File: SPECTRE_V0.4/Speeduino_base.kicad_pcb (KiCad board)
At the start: 2 copper layers, 100 x 93 mm, 172 parts, among them J1 Conn_01x04_Male, Q1 2N7002, Q10 BSP78, Q11 BSP78, Q12 BSP78, Q13 BSP78, Q14 BSP78, Q15 BSP78, Q16 BSP78, Q17 BSP78, Q18 BSP78, Q2 CJ2302, Q3 CJ2302, Q4 CJ2302, Q5 BSP78, Q6 BSP78, Q7 CJ2302, Q8 CJ2302, Q9 CJ2302, U1 MAX9926UAEE+, U2 molex_48pin, U3 LM78M05_TO220

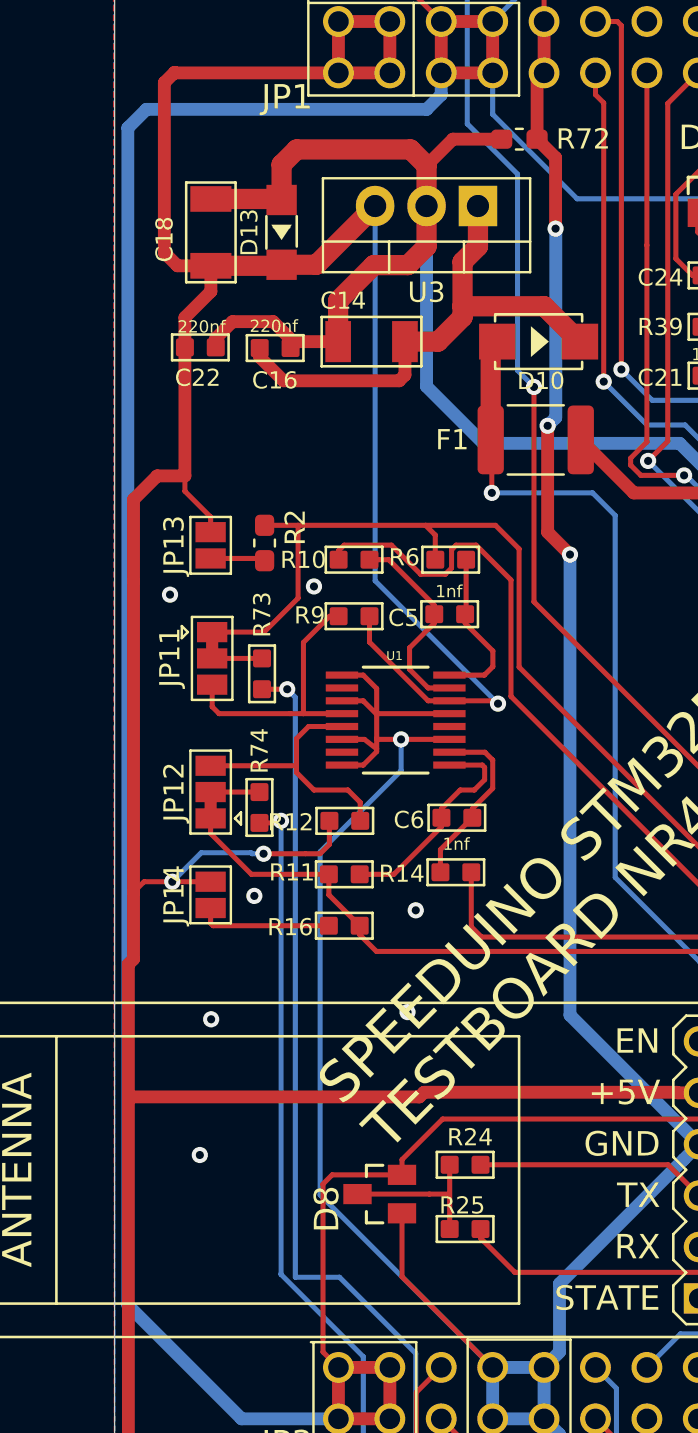
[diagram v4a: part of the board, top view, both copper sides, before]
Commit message: Add zener for safety on 3.3v. All bat54S diodes dump current on 3.3V line when driven above 3.6V therefor the 3.3V needed protection
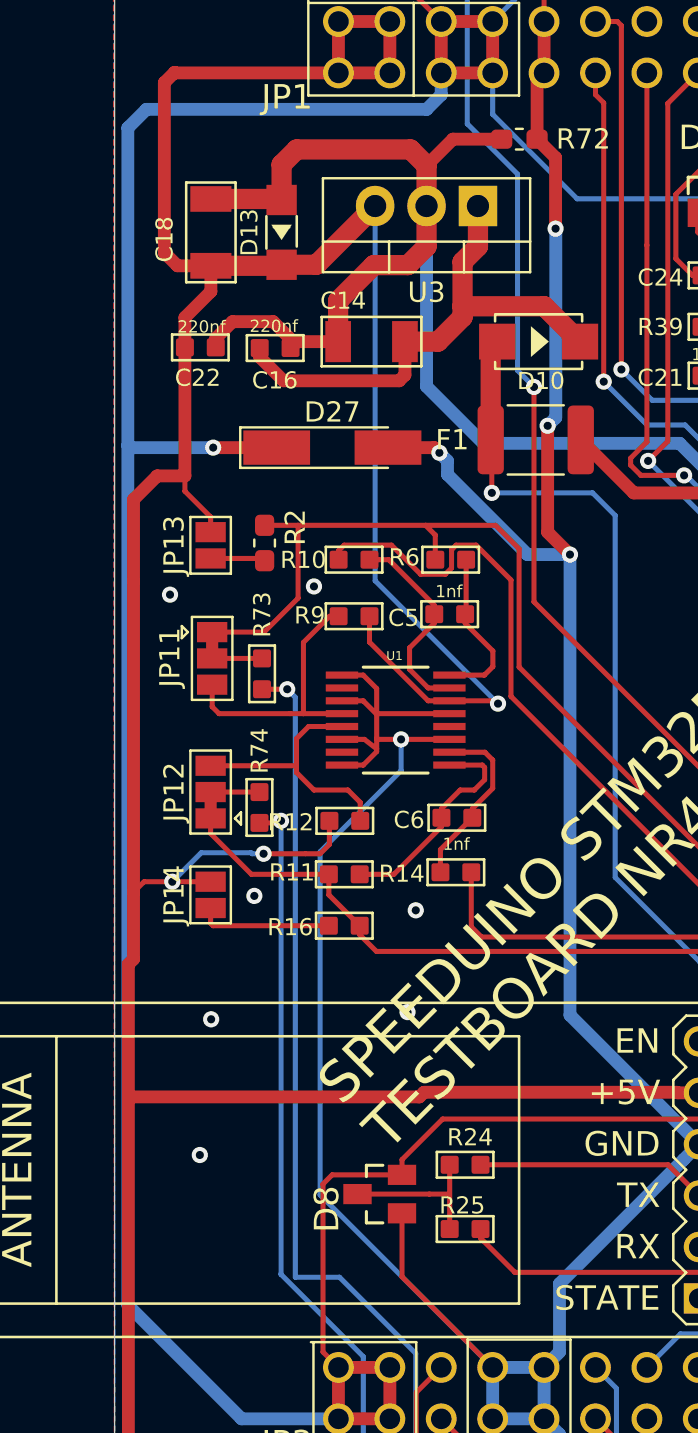
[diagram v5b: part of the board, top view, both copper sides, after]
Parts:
- added D27: 3.6V, Diode_SMD:D_MiniMELF_Handsoldering, F.Cu at (124.8, 49.8)
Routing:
- net GND: track 527.4 -> 539.0 mm, vias 41 -> 42
- net 3.3V: track 540.1 -> 547.5 mm, vias 12 -> 13
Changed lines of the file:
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@@
     (thickness 1.6)
     (drawings 31)
-    (tracks 2179)
+    (tracks 2192)
     (zones 0)
-    (modules 172)
+    (modules 173)
     (nets 173)
   )
@@
   )
   (setup
-    (last_trace_width 0.25)
+    (last_trace_width 0.635)
     (user_trace_width 0.2)
     (user_trace_width 0.45)
@@
     (add_net V_IDLE)
   )
+  (module Diode_SMD:D_MiniMELF_Handsoldering (layer Top)
+    (at 124.758 49.784)
+    (descr "Diode Mini-MELF Handsoldering")
+    (tags "Diode Mini-MELF Handsoldering")
+    (attr smd)
+    (fp_text reference D27 (at 0 -1.75) (layer F.SilkS)
+      (effects (font (size 1 1) (thickness 0.15)))
+    )
+    (fp_text value 3.6V (at 0 1.75) (layer F.Fab)
+      (effects (font (size 1 1) (thickness 0.15)))
+    )
+    (fp_line (start -4.65 1.1) (end -4.65 -1.1) (layer F.CrtYd) (width 0.05))
+    (fp_line (start 4.65 1.1) (end -4.65 1.1) (layer F.CrtYd) (width 0.05))
+    (fp_line (start 4.65 -1.1) (end 4.65 1.1) (layer F.CrtYd) (width 0.05))
+    (fp_line (start -4.65 -1.1) (end 4.65 -1.1) (layer F.CrtYd) (width 0.05))
+    (fp_line (start -0.75 0) (end -0.35 0) (layer F.Fab) (width 0.1))
+    (fp_line (start -0.35 0) (end -0.35 -0.55) (layer F.Fab) (width 0.1))
+    (fp_line (start -0.35 0) (end -0.35 0.55) (layer F.Fab) (width 0.1))
+    (fp_line (start -0.35 0) (end 0.25 -0.4) (layer F.Fab) (width 0.1))
+    (fp_line (start 0.25 -0.4) (end 0.25 0.4) (layer F.Fab) (width 0.1))
+    (fp_line (start 0.25 0.4) (end -0.35 0) (layer F.Fab) (width 0.1))
+    (fp_line (start 0.25 0) (end 0.75 0) (layer F.Fab) (width 0.1))
+    (fp_line (start -1.65 -0.8) (end 1.65 -0.8) (layer F.Fab) (width 0.1))
+    (fp_line (start -1.65 0.8) (end -1.65 -0.8) (layer F.Fab) (width 0.1))
+    (fp_line (start 1.65 0.8) (end -1.65 0.8) (layer F.Fab) (width 0.1))
+    (fp_line (start 1.65 -0.8) (end 1.65 0.8) (layer F.Fab) (width 0.1))
+    (fp_line (start -4.55 1) (end 2.75 1) (layer F.SilkS) (width 0.12))
+    (fp_line (start -4.55 -1) (end -4.55 1) (layer F.SilkS) (width 0.12))
+    (fp_line (start 2.75 -1) (end -4.55 -1) (layer F.SilkS) (width 0.12))
+    (fp_text user %R (at 0 -1.75) (layer F.Fab)
+      (effects (font (size 1 1) (thickness 0.15)))
+    )
+    (pad 2 smd rect (at 2.75 0) (size 3.3 1.7) (layers Top F.Paste F.Mask)
+      (net 1 GND))
+    (pad 1 smd rect (at -2.75 0) (size 3.3 1.7) (layers Top F.Paste F.Mask)
+      (net 66 3.3V))
+    (model ${KISYS3DMOD}/Diode_SMD.3dshapes/D_MiniMELF.wrl
+      (at (xyz 0 0 0))
+      (scale (xyz 1 1 1))
+      (rotate (xyz 0 0 0))
+    )
+  )
   (module Speeduino_base:SOT223 (layer Bottom)
     (at 190.957 69.051712 90)
@@
     (effects (font (size 0.77216 0.77216) (thickness 0.065024)) (justify left bottom))
   )
-  (via (at 210.6168 94.2848) (size 0.8) (drill 0.4) (layers Top Bottom) (net 34))
-  (via (at 206.756 97.9424) (size 0.8) (drill 0.4) (layers Top Bottom) (net 34))
   (via (at 205.3844 53.7972) (size 0.8) (drill 0.4) (layers Top Bottom) (net 0))
   (segment (start 135.22 28.73) (end 135.22 31.27) (width 0.635) (layer Top) (net 1) (status 30))
@@
   (via (at 164.6936 69.7484) (size 0.8) (drill 0.4) (layers Top Bottom) (net 1))
   (via (at 159.9184 68.6816) (size 0.8) (drill 0.4) (layers Top Bottom) (net 1))
+  (via (at 130.048 50.038) (size 0.8) (drill 0.4) (layers Top Bottom) (net 1))
+  (segment (start 127.508 49.784) (end 129.794 49.784) (width 0.635) (layer Top) (net 1))
+  (segment (start 129.794 49.784) (end 130.048 50.038) (width 0.635) (layer Top) (net 1))
+  (segment (start 134.402898 55.0672) (end 135.933915 55.0672) (width 0.635) (layer Bottom) (net 1))
+  (segment (start 130.447999 51.112301) (end 134.402898 55.0672) (width 0.635) (layer Bottom) (net 1))
+  (segment (start 130.447999 50.437999) (end 130.447999 51.112301) (width 0.635) (layer Bottom) (net 1))
+  (segment (start 135.933915 55.0672) (end 136.4996 55.0672) (width 0.635) (layer Bottom) (net 1))
+  (segment (start 130.048 50.038) (end 130.447999 50.437999) (width 0.635) (layer Bottom) (net 1))
   (segment (start 157.2717 79.121) (end 157.3021 79.0906) (width 0.25) (layer Top) (net 2))
   (segment (start 151.5872 79.0956) (end 152.5524 79.0956) (width 0.25) (layer Top) (net 2))
@@
   (segment (start 154.432 71.374) (end 155.0924 71.374) (width 0.25) (layer Top) (net 31))
   (segment (start 155.0924 71.374) (end 155.2956 71.1708) (width 0.25) (layer Top) (net 31))
+  (via (at 210.6168 94.2848) (size 0.8) (drill 0.4) (layers Top Bottom) (net 34))
+  (via (at 206.756 97.9424) (size 0.8) (drill 0.4) (layers Top Bottom) (net 34))
   (segment (start 206.883 48.217) (end 206.81 48.29) (width 0.635) (layer Bottom) (net 34) (status 30))
   (segment (start 204.27 48.29) (end 206.81 48.29) (width 1.6) (layer Bottom) (net 34) (status 30))
@@
   (segment (start 130.14 31.27) (end 130.14 32.34763) (width 0.635) (layer Bottom) (net 66))
   (segment (start 115.57 33.0708) (end 114.6556 33.9852) (width 0.635) (layer Bottom) (net 66))
-  (segment (start 114.6556 33.9852) (end 114.6556 92.1512) (width 0.635) (layer Bottom) (net 66))
   (segment (start 114.6556 92.1512) (end 120.2744 97.77) (width 0.635) (layer Bottom) (net 66))
   (via (at 146.2024 37.4904) (size 0.8) (drill 0.4) (layers Top Bottom) (net 66))
@@
   (segment (start 120.9548 25.5016) (end 120.9548 23.7744) (width 0.25) (layer Top) (net 66))
   (segment (start 127.9784 26.5684) (end 122.0216 26.5684) (width 0.25) (layer Top) (net 66))
+  (via (at 118.872 49.784) (size 0.8) (drill 0.4) (layers Top Bottom) (net 66))
+  (segment (start 122.008 49.784) (end 118.872 49.784) (width 0.635) (layer Top) (net 66))
+  (segment (start 114.6556 49.6824) (end 114.7572 49.784) (width 0.635) (layer Bottom) (net 66))
+  (segment (start 114.7572 49.784) (end 118.872 49.784) (width 0.635) (layer Bottom) (net 66))
+  (segment (start 114.6556 49.6824) (end 114.6556 92.1512) (width 0.635) (layer Bottom) (net 66))
+  (segment (start 114.6556 33.9852) (end 114.6556 49.6824) (width 0.635) (layer Bottom) (net 66))
   (segment (start 199.19 78.35) (end 184.159 78.35) (width 0.25) (layer Top) (net 67) (status 10))
   (segment (start 184.159 78.35) (end 178.3932 78.35) (width 0.25) (layer Top) (net 67))
@@
   )
   (zone (net 34) (net_name PWR_GND) (layer Bottom) (hatch edge 0.508)
-    (connect_pads yes (clearance 0.254))
+    (connect_pads (clearance 0.254))
     (min_thickness 0.254)
     (fill yes (arc_segments 32) (thermal_gap 0.508) (thermal_bridge_width 0.508))
@@
   )
   (zone (net 34) (net_name PWR_GND) (layer Top) (hatch edge 0.508)
-    (connect_pads yes (clearance 0.254))
+    (connect_pads (clearance 0.254))
     (min_thickness 0.254)
     (fill yes (arc_segments 32) (thermal_gap 0.508) (thermal_bridge_width 0.508))
@@
   (zone (net 1) (net_name GND) (layer Top) (hatch edge 0.508)
     (priority 1)
-    (connect_pads yes (clearance 0.254))
+    (connect_pads (clearance 0.254))
     (min_thickness 0.254)
     (fill yes (arc_segments 32) (thermal_gap 0.508) (thermal_bridge_width 0.508))
@@
   (zone (net 1) (net_name GND) (layer Bottom) (hatch edge 0.508)
     (priority 1)
-    (connect_pads yes (clearance 0.254))
+    (connect_pads (clearance 0.254))
     (min_thickness 0.254)
     (fill yes (arc_segments 32) (thermal_gap 0.508) (thermal_bridge_width 0.508))

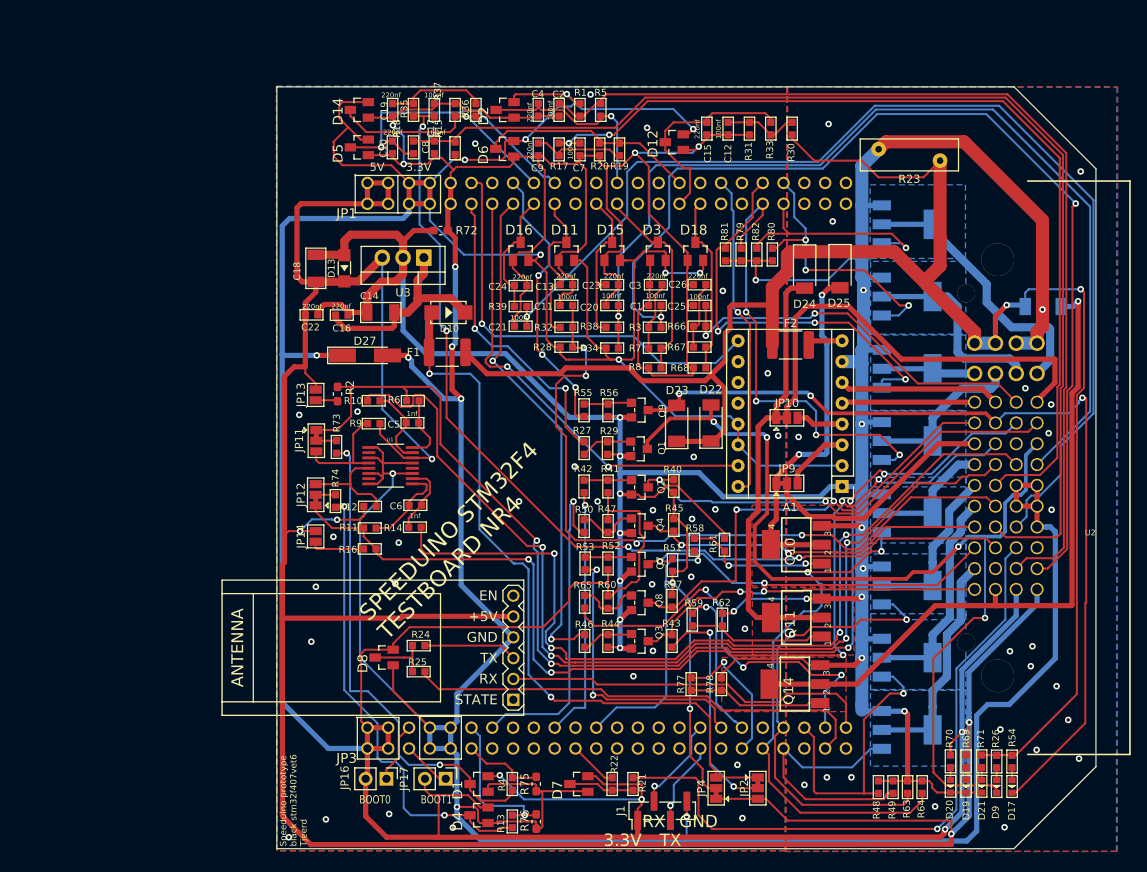
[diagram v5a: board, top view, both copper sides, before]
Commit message: add canbus driver add 3d models to components for 3d render.
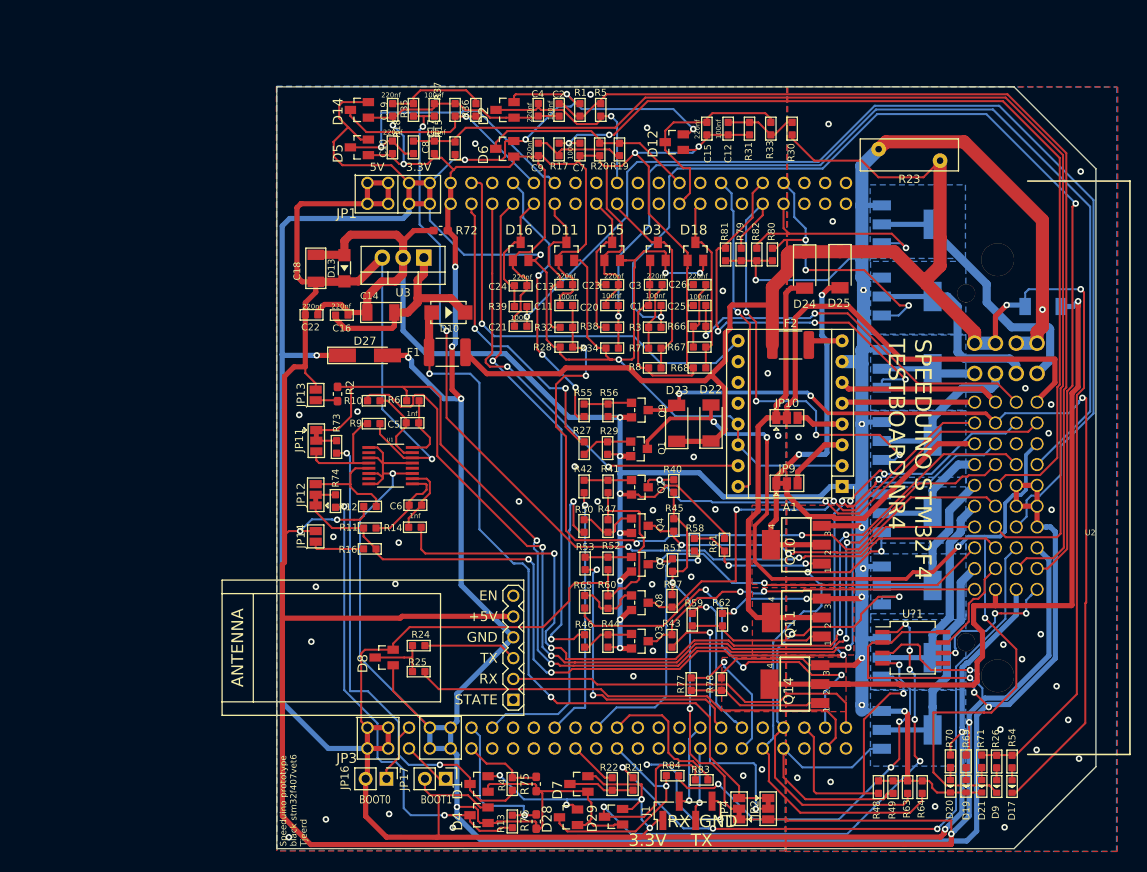
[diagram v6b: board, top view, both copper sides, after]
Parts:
- added D28: BAT54S, Speeduino_base:SOT23, F.Cu at (149.6, 106.2)
- added D29: BAT54S, Speeduino_base:SOT23, F.Cu at (155.1, 106.1)
- added R83: 1k, Speeduino_base:R0603, F.Cu at (165.9, 101.6)
- added R84: 1K, Speeduino_base:R0603, F.Cu at (162.3, 101.1)
- added U?1: TJA1050, Package_SO:SO-8_5.3x6.2mm_P1.27mm, F.Cu at (191.6, 85.5)
- D22, D23, D24, D25, D26: footprint Diode_SMD:D_SOD-128 -> Speeduino_base:D_SOD-128
- moved JP4 3.76 mm to (170.4, 105.1)
- moved J1 3.08 mm to (164.1, 105.4)
- moved JP2 2.81 mm to (174.0, 105.1)
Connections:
- U2 pad 37: Net-(U2-Pad37) -> 5V
- U2 pad 43: Net-(U2-Pad43) -> CANH
- U2 pad 45: 5V -> CANL
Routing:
- net Net-(D29-Pad3): track 0.00 -> 83.3 mm, vias 0 -> 6
- net GND: track 539.0 -> 591.8 mm, vias 42 -> 46
- net Net-(R84-Pad2): track 0.00 -> 47.8 mm, vias 0 -> 4
- net PD0: track 0.00 -> 26.7 mm, vias 0 -> 1
- net 5V: track 342.6 -> 364.5 mm, vias 5 -> 6
- net CANL: track 0.00 -> 18.8 mm, vias 0 -> 3
- net PD1: track 0.00 -> 17.5 mm
- net CANH: track 0.00 -> 12.4 mm
- net BOOST-OUT: track 82.6 -> 93.1 mm
- net 3.3V: track 547.5 -> 555.4 mm, vias 13 -> 15
- net FUEL_PUMP: track 123.1 -> 129.4 mm
- net Net-(JP2-Pad2): track 28.4 -> 33.9 mm
- net Net-(JP4-Pad2): track 43.3 -> 47.8 mm
- net VBAT_F1: track 90.0 -> 92.1 mm
- net FLEX_FUEL_IN: track 80.5 -> 81.8 mm, vias 1 -> 3
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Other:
- rule trace_min: 0.2 -> 0.25

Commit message: rs232 header NRF
Added rs232 driver and Added NRF header to use SPI .
TODO:
- finish rs232 to 48 pin connector
- route BME280
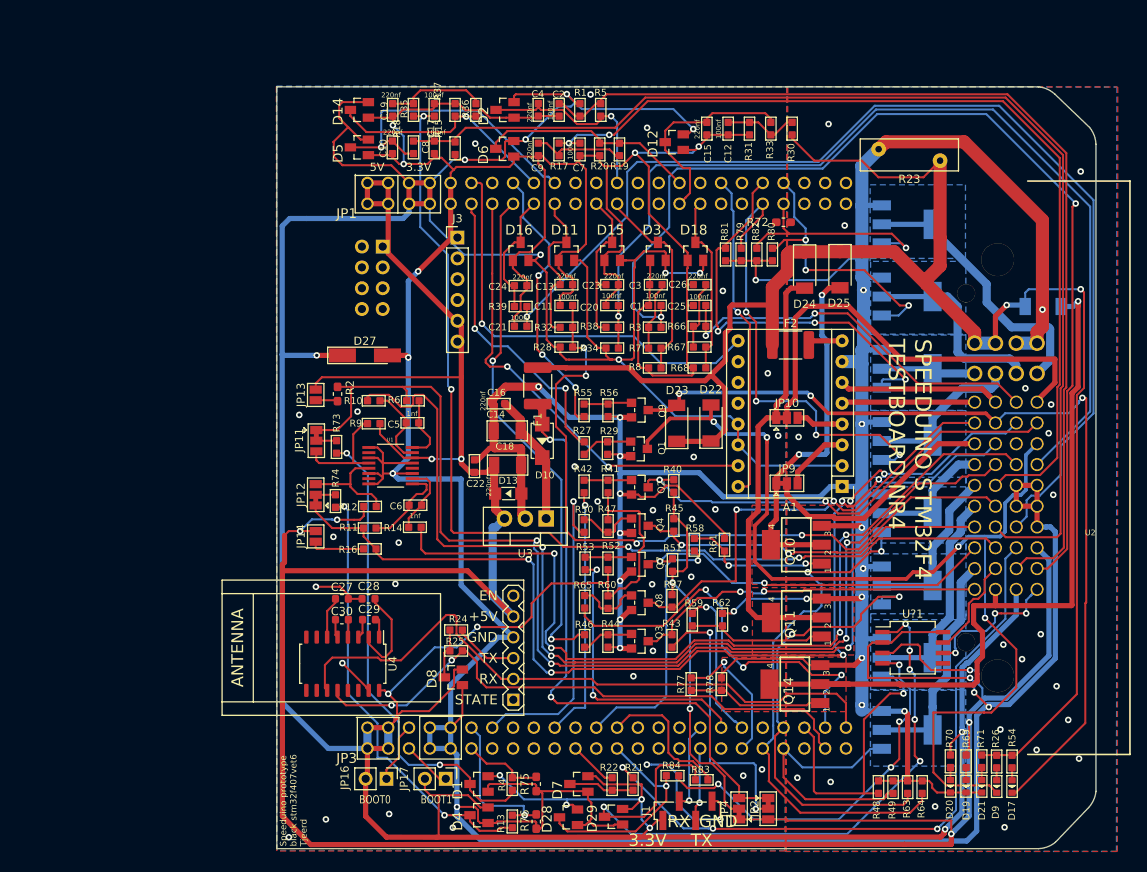
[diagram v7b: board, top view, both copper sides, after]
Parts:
- added C27: 100nF, Capacitor_SMD:C_0603_1608Metric, F.Cu at (121.9, 79.5)
- added C28: 100nF, Capacitor_SMD:C_0603_1608Metric, F.Cu at (125.2, 79.5)
- added C29: 100nF, Capacitor_SMD:C_0603_1608Metric, F.Cu at (125.2, 82.0)
- added C30: 100nF, Capacitor_SMD:C_0603_1608Metric, F.Cu at (121.9, 82.0)
- added J2: Conn_02x04_Odd_Even, Speeduino_base:PinHeader_2x04_P2.54mm_Vertical, B.Cu at (126.9, 36.5)
- added J3: Conn_01x06_Male, Connector_PinHeader_2.54mm:PinHeader_1x06_P2.54mm_Vertical, F.Cu at (136.1, 35.4)
- added U4: MAX3232, Package_SO:SOIC-16_4.55x10.3mm_P1.27mm, F.Cu at (122.0, 87.4)
- moved R72 41.9 mm to (175.8, 33.5), turned to 0 degrees
- moved U3 35.2 mm to (146.9, 69.7)
- moved D13 34.0 mm to (142.2, 66.7), turned to 180 degrees
- moved C18 33.6 mm to (142.2, 63.2), turned to 180 degrees
- moved C22 27.1 mm to (138.1, 63.3), turned to 0 degrees
- moved C16 22.0 mm to (141.1, 55.7), turned to 90 degrees
- moved C14 21.1 mm to (142.1, 59.0)
- moved D10 19.4 mm to (146.4, 60.2), turned to 270 degrees
- moved F1 11.8 mm to (145.8, 53.5), turned to 270 degrees
- moved D8 8.79 mm to (135.6, 89.1)
- moved R25 5.23 mm to (135.9, 85.9)
- moved R24 4.95 mm to (135.9, 83.3)
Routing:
- net PWR_GND: track 390.6 -> 353.2 mm, vias 38 -> 39
- net PD8: track 45.7 -> 79.1 mm
- net GND: track 591.8 -> 565.6 mm, vias 46 -> 43
- net VBAT_F1: track 92.1 -> 74.3 mm
- net PD9: track 56.9 -> 70.9 mm, vias 0 -> 2
- net Net-(C28-Pad1): track 0.00 -> 11.8 mm
- net VBAT: track 223.0 -> 212.8 mm
- net Net-(C14-Pad2): track 25.6 -> 16.1 mm
- net MAP: track 116.6 -> 124.3 mm
- net 3.3V: track 555.4 -> 563.0 mm, vias 15 -> 17
- net 5V: track 364.5 -> 357.4 mm, vias 6 -> 7
- net VR1+: track 142.6 -> 148.9 mm
- net VR1-: track 120.3 -> 126.3 mm
- net Net-(C27-Pad1): track 0.00 -> 5.10 mm
- net /BT_TX: track 11.4 -> 7.90 mm
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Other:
- outline, holes or cut-outs redrawn
